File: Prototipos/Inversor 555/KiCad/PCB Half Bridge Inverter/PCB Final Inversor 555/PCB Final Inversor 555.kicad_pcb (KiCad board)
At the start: 2 copper layers, 50 x 100 mm, 22 parts, among them Q1 IRFZ44, Q2 IRFZ44, Q3 BC548, U1 TLC555xD, U2 LM7809_TO220

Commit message: Modificaciones en PCB
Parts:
- moved R4 50.3 mm to (80.0, 134.0), turned to 0 degrees
- moved Q2 24.3 mm to (79.8, 115.0), turned to -90 degrees
- moved C5 22.0 mm to (68.5, 120.0)
- moved R3 20.0 mm to (76.1, 113.0)
- moved U2 18.1 mm to (79.8, 92.5), turned to -90 degrees
- moved C3 18.0 mm to (73.5, 106.0)
- moved Q3 12.6 mm to (90.5, 128.4)
- moved Q1 9.48 mm to (79.8, 104.0), turned to -90 degrees
- moved C1 8.25 mm to (89.0, 82.0)
- moved C2 8.02 mm to (89.0, 86.0)
- moved R1 5.58 mm to (83.0, 88.0), turned to 90 degrees
- moved U1 5.11 mm to (88.0, 66.0)
- moved R8 2.94 mm to (61.0, 109.3), turned to 90 degrees
- moved R7 2.50 mm to (64.0, 101.7)
- moved R2 1.80 mm to (74.0, 76.0)
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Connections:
- R2 pad 3: (no net) -> Net-(U1-THR)
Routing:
- net 555: track 0.00 -> 122.4 mm
- net AGND: track 0.00 -> 52.4 mm
- net Net-(Q1-G): track 0.00 -> 46.5 mm
- net Net-(U1-THR): track 0.00 -> 39.2 mm
- net 12Vdc: track 64.1 -> 101.2 mm, vias 0 -> 2
- net Net-(Q2-G): track 0.00 -> 31.9 mm
- net Net-(U1-CV): track 0.00 -> 14.6 mm
- net Net-(C3-Pad2): track 0.00 -> 14.0 mm
- net Net-(Q1-D): track 0.00 -> 13.5 mm
- net 3,3Vdc: track 0.00 -> 12.7 mm
- net Module_ident: track 0.00 -> 11.2 mm
- net Net-(Q1-S): track 0.00 -> 9.93 mm
- net PGND: track 173.6 -> 165.0 mm
- net Net-(Q3-B): track 0.00 -> 6.06 mm
- added copper zone on B.Cu, net 12Vdc
- added copper zone on B.Cu, net 555
- added copper zone on B.Cu, net AGND
- added copper zone on B.Cu, net Net-(C3-Pad2)
- added copper zone on B.Cu, net PGND

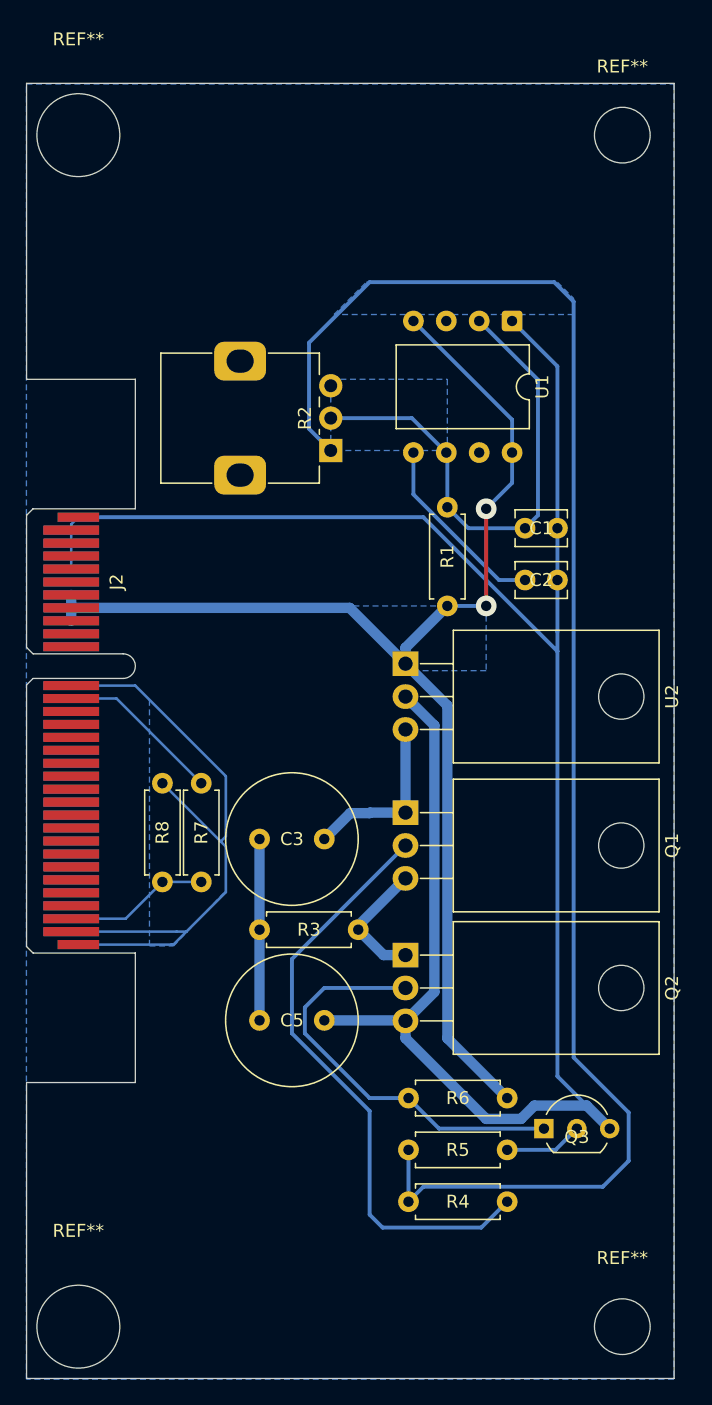
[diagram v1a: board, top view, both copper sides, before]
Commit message: Agregar resistencia en seria a potenciometro
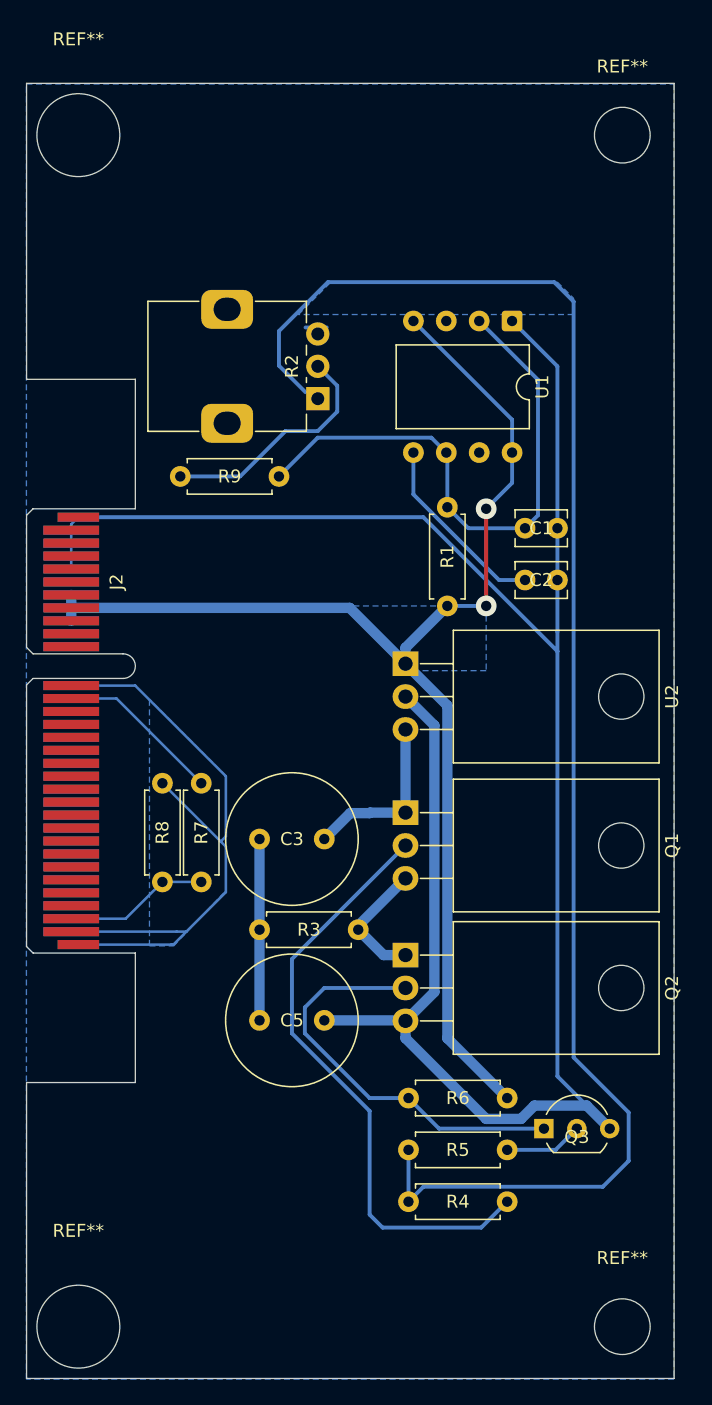
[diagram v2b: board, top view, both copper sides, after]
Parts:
- added R9: 120k, Resistor_THT:R_Axial_DIN0207_L6.3mm_D2.5mm_P7.62mm_Horizontal, F.Cu at (70.0, 78.0)
- R2: value 144.3K -> 50k
- moved R2 4.12 mm to (73.0, 72.0)
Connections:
- R2 pad 2: Net-(U1-THR) -> Net-(R2-Pad2)
- R2 pad 3: Net-(U1-THR) -> Net-(R2-Pad2)
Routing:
- net Net-(R2-Pad2): track 0.00 -> 20.0 mm
- net Net-(U1-THR): track 39.2 -> 43.9 mm
- net 555: track 122.4 -> 120.9 mm
- removed copper zone on B.Cu, net Net-(C3-Pad2)

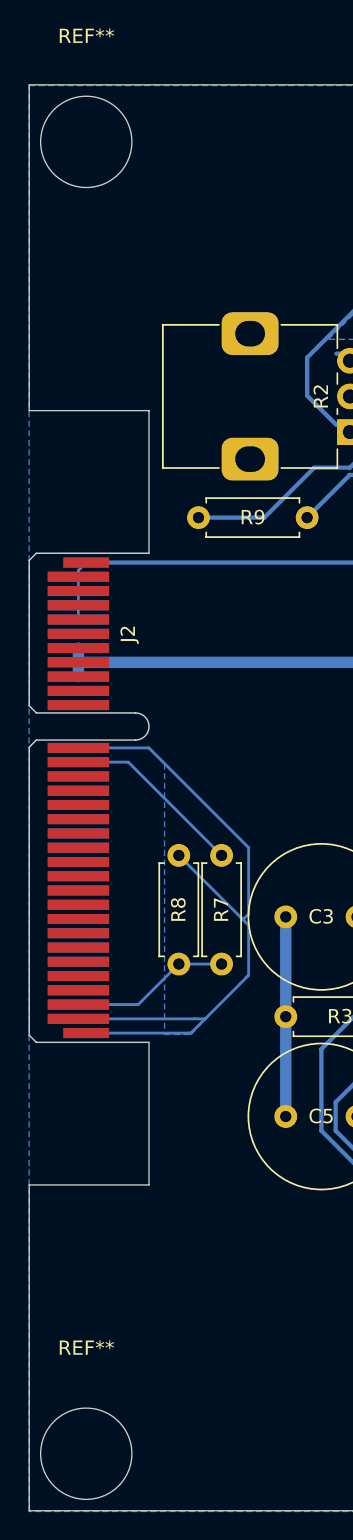
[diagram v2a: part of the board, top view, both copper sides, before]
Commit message: Agregar corrección de zona de relleno
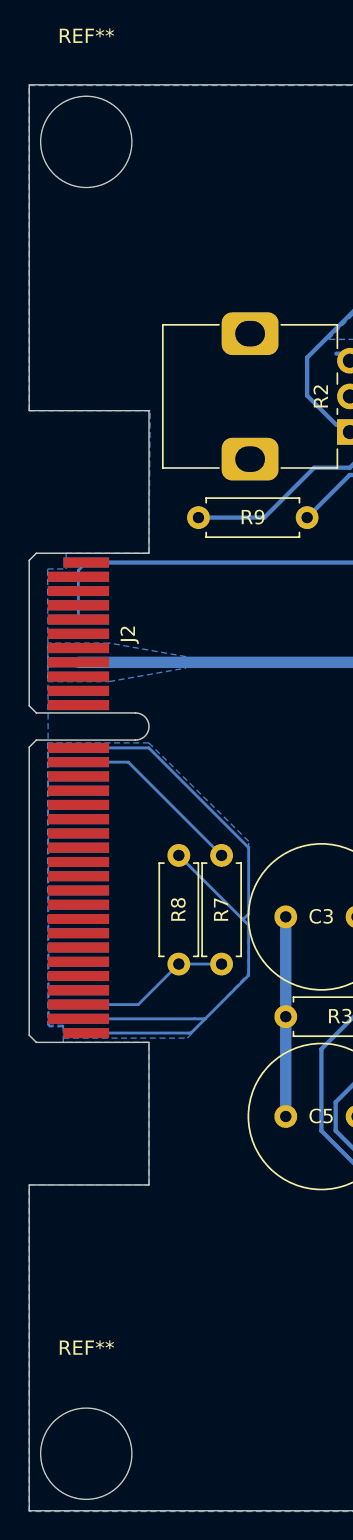
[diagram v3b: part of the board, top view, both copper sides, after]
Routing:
- net 12Vdc: track 101.2 -> 99.2 mm
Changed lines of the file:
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@@
-	)
-	(segment
-		(start 53.96 87.15)
-		(end 53.96 89.15)
-		(width 0.8)
-		(layer "B.Cu")
-		(net 17)
 	)
 	(segment
@@
 		(polygon
 			(pts
-				(xy 60 114.25) (xy 61.872223 114.25) (xy 65.9 109.985295) (xy 65.9 101.15) (xy 60 95.25)
+				(xy 51.81 113.6) (xy 52.91 113.6) (xy 52.91 114.5) (xy 61.606112 114.5) (xy 65.87 109.985295) (xy 65.9 100.7)
+				(xy 58.9 93.8) (xy 51.81 93.8)
 			)
 		)
@@
 	)
 	(zone
+		(net 17)
+		(net_name "12Vdc")
+		(layer "B.Cu")
+		(hatch edge 0.5)
+		(priority 2)
+		(connect_pads yes
+			(clearance 0.1)
+		)
+		(min_thickness 0.3)
+		(filled_areas_thickness no)
+		(fill yes
+			(thermal_gap 0.5)
+			(thermal_bridge_width 0.5)
+		)
+		(polygon
+			(pts
+				(xy 51.816 86.8) (xy 51.81 89.5) (xy 56.1086 89.5) (xy 61.5 88.55) (xy 61.5 87.75) (xy 56.115847 86.8)
+			)
+		)
+	)
+	(zone
 		(net 11)
 		(net_name "PGND")
@@
 		(polygon
 			(pts
-				(xy 50.5 47.7) (xy 100.5 47.7) (xy 100.5 147.7) (xy 50.5 147.7)
-			)
-		)
+				(xy 50.5 124.8) (xy 58.9 124.8) (xy 58.9 114.8) (xy 52.9 114.8) (xy 52.9 113.7) (xy 51.896687 113.70001)
+				(xy 51.8 81.6) (xy 53.1 81.6) (xy 53.1 80.5) (xy 58.9 80.5) (xy 59 70.5) (xy 50.5 70.5) (xy 50.5 47.7)
+				(xy 100.5 47.7) (xy 100.5 147.7) (xy 50.5 147.7)
+			)
+		)

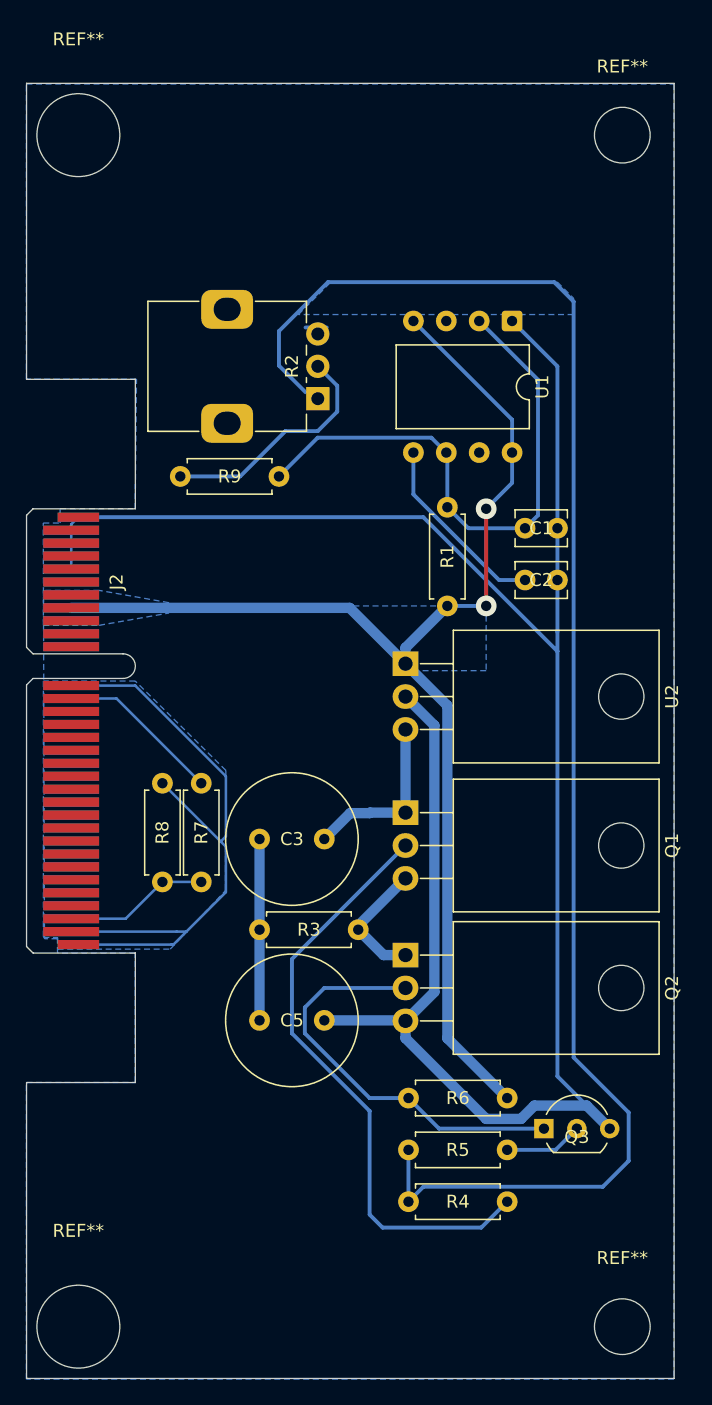
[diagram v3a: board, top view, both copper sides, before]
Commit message: Agregar test point
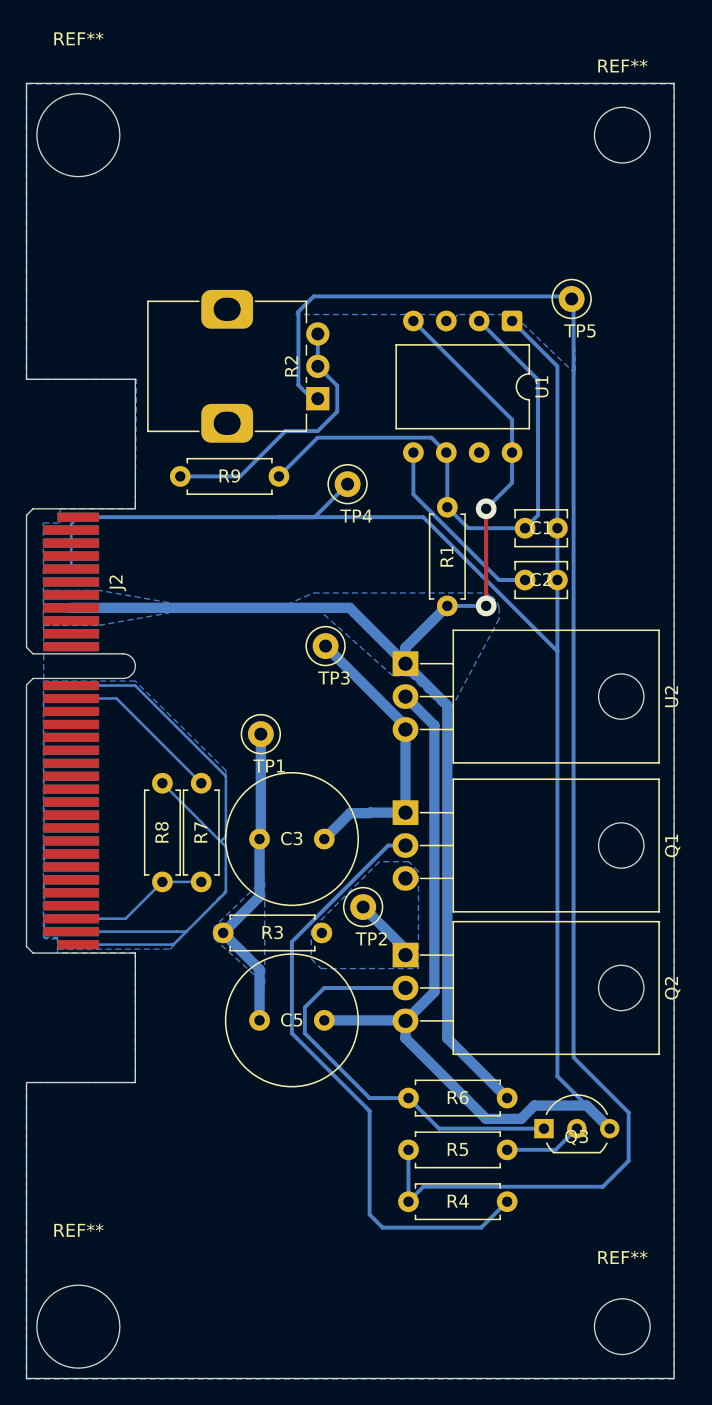
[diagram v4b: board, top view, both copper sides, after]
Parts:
- added TP1: TestPoint, TestPoint:TestPoint_Loop_D1.80mm_Drill1.0mm_Beaded, F.Cu at (68.6, 97.9)
- added TP2: TestPoint, TestPoint:TestPoint_Loop_D1.80mm_Drill1.0mm_Beaded, F.Cu at (76.5, 111.2)
- added TP3: TestPoint, TestPoint:TestPoint_Loop_D1.80mm_Drill1.0mm_Beaded, F.Cu at (73.6, 91.1)
- added TP4: TestPoint, TestPoint:TestPoint_Loop_D1.80mm_Drill1.0mm_Beaded, F.Cu at (75.3, 78.6)
- added TP5: TestPoint, TestPoint:TestPoint_Loop_D1.80mm_Drill1.0mm_Beaded, F.Cu at (92.6, 64.3)
- moved R3 2.82 mm to (73.3, 113.2)
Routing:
- net Net-(C3-Pad2): track 14.0 -> 24.5 mm
- net Net-(Q1-D): track 13.5 -> 22.5 mm
- net PGND: track 165.0 -> 171.4 mm
- net Net-(Q1-S): track 9.93 -> 5.06 mm
- net 555: track 120.9 -> 119.9 mm
- net Net-(R2-Pad2): track 20.0 -> 20.8 mm
- net Net-(Q1-G): track 46.5 -> 47.3 mm
- added copper zone on B.Cu, net Net-(C3-Pad2)
- added copper zone on B.Cu, net Net-(Q1-S)

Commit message: Agregar correcciones finales PCB
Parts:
- moved TP1 1.50 mm to (68.6, 96.4)
- moved C5 0.60 mm to (68.5, 120.6)
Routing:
- net Net-(C3-Pad2): track 24.5 -> 26.0 mm
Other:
- board text added: "Driver de MOSFETs"
- board text added: "Ident. módulo"
- board text added: "Medio puente"
- board text added: "Oscilador 555"
- board text added: "Regulador 9 V"
